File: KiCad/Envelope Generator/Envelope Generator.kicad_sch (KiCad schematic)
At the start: 43 parts, among them J1 Screw_Terminal_01x03, J2 Screw_Terminal_01x03, U1 TL074, U2 TL074, U3 TL074

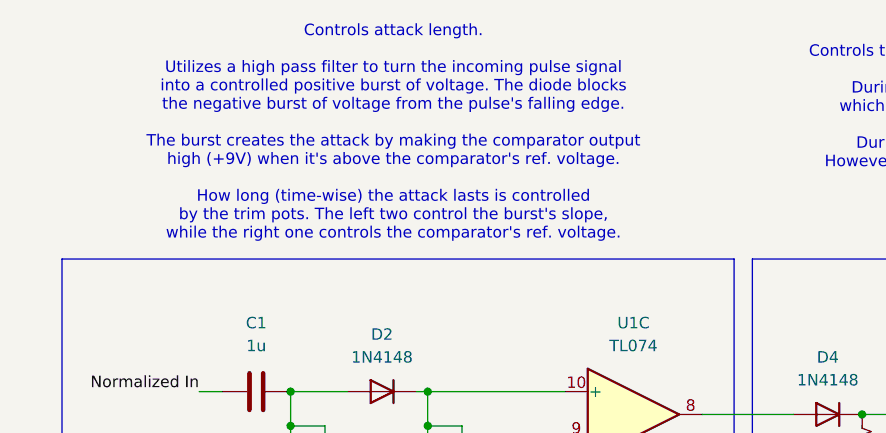
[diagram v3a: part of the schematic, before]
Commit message: fixed power board, replaced sketchy voltage divider - op amp cct. with an LDO to product +5V
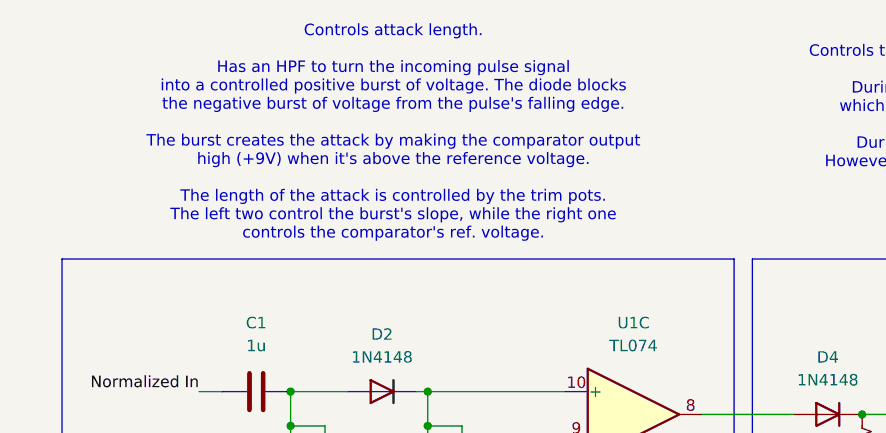
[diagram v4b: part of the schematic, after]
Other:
- note added: "Controls attack length. Has an HPF to turn the incoming pulse signal into a controlled positive burst of voltage. The diode blocks the negative burst of voltage from the pulse's falling edge. The burst creates the attack by making the comparator output high (+9V) when it's above the reference voltage. The length of the attack is controlled by the trim pots. The left two control the burst's slope,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"
- note removed: "Controls attack length. Utilizes a high pass filter to turn the incoming pulse signal into a controlled positive burst of voltage. The diode blocks the negative burst of voltage from the pulse's falling edge. The burst creates the attack by making the comparator output high (+9V) when it's above the comparator's ref. voltage. How long (time-wise) the attack lasts is controlled by the trim pots. T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"
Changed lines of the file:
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@@
 		)
 	)
-	(text "Controls attack length.\n\nUtilizes a high pass filter to turn the incoming pulse signal\ninto a controlled positive burst of voltage. The diode blocks\nthe negative burst of voltage from the pulse's falling edge.\n\nThe burst creates the attack by making the comparator output\nhigh (+9V) when it's above the comparator's ref. voltage.\n\nHow long (time-wise) the attack lasts is controlled\nby the trim pots. The left two control the burst's slope,\nwhile the right one controls the comparator's ref. voltage."
+	(text "Controls attack length.\n\nHas an HPF to turn the incoming pulse signal\ninto a controlled positive burst of voltage. The diode blocks\nthe negative burst of voltage from the pulse's falling edge.\n\nThe burst creates the attack by making the comparator output\nhigh (+9V) when it's above the reference voltage.\n\nThe length of the attack is controlled by the trim pots.\nThe left two control the burst's slope, while the right one\ncontrols the comparator's ref. voltage."
 		(exclude_from_sim no)
 		(at 59.69 27.178 0)

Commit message: finished separating into separate kicad projects
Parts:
- removed R1, R2: 100k, symbol Device:R_US
- added RV1: 100k, Potentiometer_THT:Potentiometer_Bourns_3296W_Vertical, symbol Device:R_Potentiometer_Trim_US
- renumbered R3 to R1, R4 to R2, R5 to R3, R6 to R4, R7 to R5, R8 to R6, R9 to R7, R10 to R8, RV9 to RV10, RV10 to RV11, RV11 to RV12, RV12 to RV13, RV13 to RV14, RV14 to RV15, RV1 to RV2, RV2 to RV3, RV3 to RV4, RV4 to RV5, RV5 to RV6, RV6 to RV7, RV7 to RV8, RV8 to RV9
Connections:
- net -9V: now also RV1.1
- net GND: now also RV1.3
- net at U1.2 (-): now also RV1.2
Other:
- note added: "Ref. voltage should be between -5V and -0.5V, however in case that's wrong, it's adjustable."
- note added: "Turns the input into a binary signal, low is 0V and high is 9V. This is needed because the input is not a binary signal, instead it is either -5V or a range between ~0V to ~2.5V since the input also serves as the oscillator's control voltage."
- note removed: "Trigger above -4.5V"
- note removed: "Turns the input into a binary signal, low is 0V and high is 9V. This is because the input is not a binary signal, instead it is either -9V or a range between ~0V to ~2.5V since the input also serves as the oscillator's control voltage."

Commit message: added test points
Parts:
- added TP? (x14): TestPoint_Small, symbol Connector:TestPoint_Small
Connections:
- net Amp Out: now also TP?.1
- net Amp Sustain/Base Voltage: now also TP?.1
- net Amp Target Voltage: now also TP?.1
- net Filter Out: now also TP?.1
- net Filter Sustain/Base Voltage: now also TP?.1
- net Filter Target Voltage: now also TP?.1
- net GND: now also TP?.1
- net In: now also TP?.1
- net Normalized In: now also TP?.1
- net Unscaled Amp Out: now also TP?.1
- net Unscaled Filter Out: now also TP?.1
- net Filter Burst: now reaches D5.2 (A), U1.7
- net Filter Burst: now also TP?.1
- net Input Comparator Ref: now reaches RV1.2, U1.2 (-)
- net Input Comparator Ref: now also TP?.1
- net Amp Burst: now reaches D4.2 (A), U1.8
- net Amp Burst: now also TP?.1
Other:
- moved on the sheet: C3, D1, R1, RV1, RV8, RV9, U1A, U1D

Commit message: added power indicator LEDs
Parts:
- gave numbers to parts that had none: 14
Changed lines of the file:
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@@
 		(dnp no)
 		(fields_autoplaced yes)
-		(property "Reference" "TP?"
+		(property "Reference" "TP10"
 			(at 194.31 153.6699 0)
 			(hide yes)
@@
 			(project "Envelope Generator"
 				(path "/f00ec82e-7fb8-4c7e-bfac-cc036a335e43"
-					(reference "TP?")
+					(reference "TP10")
 					(unit 1)
 				)
@@
 		(dnp no)
 		(fields_autoplaced yes)
-		(property "Reference" "TP?"
+		(property "Reference" "TP6"
 			(at 143.51 173.9899 0)
 			(hide yes)
@@
 			(project "Envelope Generator"
 				(path "/f00ec82e-7fb8-4c7e-bfac-cc036a335e43"
-					(reference "TP?")
+					(reference "TP6")
 					(unit 1)
 				)
@@
 		(dnp no)
 		(fields_autoplaced yes)
-		(property "Reference" "TP?"
+		(property "Reference" "TP4"
 			(at 97.79 160.0199 0)
 			(hide yes)
@@
 			(project "Envelope Generator"
 				(path "/f00ec82e-7fb8-4c7e-bfac-cc036a335e43"
-					(reference "TP?")
+					(reference "TP4")
 					(unit 1)
 				)
@@
 		(dnp no)
 		(fields_autoplaced yes)
-		(property "Reference" "TP?"
+		(property "Reference" "TP1"
 			(at 36.83 163.8299 0)
 			(hide yes)
@@
 			(project "Envelope Generator"
 				(path "/f00ec82e-7fb8-4c7e-bfac-cc036a335e43"
-					(reference "TP?")
+					(reference "TP1")
 					(unit 1)
 				)
@@
 		(dnp no)
 		(fields_autoplaced yes)
-		(property "Reference" "TP?"
+		(property "Reference" "TP13"
 			(at 227.33 132.0799 0)
 			(hide yes)
@@
 			(project "Envelope Generator"
 				(path "/f00ec82e-7fb8-4c7e-bfac-cc036a335e43"
-					(reference "TP?")
+					(reference "TP13")
 					(unit 1)
 				)
@@
 		(dnp no)
 		(fields_autoplaced yes)
-		(property "Reference" "TP?"
+		(property "Reference" "TP2"
 			(at 96.52 57.1499 0)
 			(hide yes)
@@
 			(project "Envelope Generator"
 				(path "/f00ec82e-7fb8-4c7e-bfac-cc036a335e43"
-					(reference "TP?")
+					(reference "TP2")
 					(unit 1)
 				)
@@
 		(dnp no)
 		(fields_autoplaced yes)
-		(property "Reference" "TP?"
+		(property "Reference" "TP9"
 			(at 194.31 151.1299 0)
 			(hide yes)
@@
 			(project "Envelope Generator"
 				(path "/f00ec82e-7fb8-4c7e-bfac-cc036a335e43"
-					(reference "TP?")
+					(reference "TP9")
 					(unit 1)
 				)
@@
 		(dnp no)
 		(fields_autoplaced yes)
-		(property "Reference" "TP?"
+		(property "Reference" "TP5"
 			(at 143.51 148.5899 0)
 			(hide yes)
@@
 			(project "Envelope Generator"
 				(path "/f00ec82e-7fb8-4c7e-bfac-cc036a335e43"
-					(reference "TP?")
+					(reference "TP5")
 					(unit 1)
 				)
@@
 		(dnp no)
 		(fields_autoplaced yes)
-		(property "Reference" "TP?"
+		(property "Reference" "TP12"
 			(at 227.33 76.1999 0)
 			(hide yes)
@@
 			(project "Envelope Generator"
 				(path "/f00ec82e-7fb8-4c7e-bfac-cc036a335e43"
-					(reference "TP?")
+					(reference "TP12")
 					(unit 1)
 				)
@@
 		(dnp no)
 		(fields_autoplaced yes)
-		(property "Reference" "TP?"
+		(property "Reference" "TP14"
 			(at 234.442 153.6699 0)
 			(hide yes)
@@
 			(project "Envelope Generator"
 				(path "/f00ec82e-7fb8-4c7e-bfac-cc036a335e43"
-					(reference "TP?")
+					(reference "TP14")
 					(unit 1)
 				)
@@
 		(dnp no)
 		(fields_autoplaced yes)
-		(property "Reference" "TP?"
+		(property "Reference" "TP11"
 			(at 194.31 156.2099 0)
 			(hide yes)
@@
 			(project "Envelope Generator"
 				(path "/f00ec82e-7fb8-4c7e-bfac-cc036a335e43"
-					(reference "TP?")
+					(reference "TP11")
 					(unit 1)
 				)
@@
 		(dnp no)
 		(fields_autoplaced yes)
-		(property "Reference" "TP?"
+		(property "Reference" "TP7"
 			(at 158.75 59.6899 0)
 			(hide yes)
@@
 			(project "Envelope Generator"
 				(path "/f00ec82e-7fb8-4c7e-bfac-cc036a335e43"
-					(reference "TP?")
+					(reference "TP7")
 					(unit 1)
 				)
@@
 		(dnp no)
 		(fields_autoplaced yes)
-		(property "Reference" "TP?"
+		(property "Reference" "TP8"
 			(at 160.02 115.5699 0)
 			(hide yes)
@@
 			(project "Envelope Generator"
 				(path "/f00ec82e-7fb8-4c7e-bfac-cc036a335e43"
-					(reference "TP?")
+					(reference "TP8")
 					(unit 1)
 				)
@@
 		(dnp no)
 		(fields_autoplaced yes)
-		(property "Reference" "TP?"
+		(property "Reference" "TP3"
 			(at 96.52 113.0299 0)
 			(hide yes)
@@
 			(project "Envelope Generator"
 				(path "/f00ec82e-7fb8-4c7e-bfac-cc036a335e43"
-					(reference "TP?")
+					(reference "TP3")
 					(unit 1)
 				)

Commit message: updated footprints in envelope generator
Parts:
- C3: footprint (none) -> Capacitor_SMD:C_0805_2012Metric
- J1, J2: footprint (none) -> Header 691137710003:691137710003
- R1, R4, R5, R6, R7, R8: footprint (none) -> Resistor_SMD:R_0805_2012Metric
- R2, R3: footprint Resistor_SMD:R_0603_1608Metric -> Resistor_SMD:R_0805_2012Metric
- RV1, RV6, RV7: footprint Potentiometer_THT:Potentiometer_Bourns_3296W_Vertical -> Potentiometer_THT:Potentiometer_Bourns_3339P_Vertical
- RV10, RV11, RV12, RV13, RV14, RV15, RV2, RV3, RV4, RV5: footprint (none) -> Potentiometer_THT:Potentiometer_Bourns_3339P_Vertical
- RV8, RV9: footprint Potentiometer_SMD:Potentiometer_Bourns_TC33X_Vertical -> Potentiometer_THT:Potentiometer_Bourns_3339P_Vertical
- TP1, TP10, TP11, TP12, TP13, TP14, TP2, TP3, TP4, TP5, TP6, TP7, TP8, TP9: footprint (none) -> TestPoint:TestPoint_Keystone_5000-5004_Miniature
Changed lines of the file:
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@@
 			)
 		)
-		(property "Footprint" "Potentiometer_SMD:Potentiometer_Bourns_TC33X_Vertical"
+		(property "Footprint" "Potentiometer_THT:Potentiometer_Bourns_3339P_Vertical"
 			(at 142.24 160.02 0)
 			(hide yes)
@@
 			)
 		)
-		(property "Footprint" ""
+		(property "Footprint" "Resistor_SMD:R_0805_2012Metric"
 			(at 189.484 52.324 90)
 			(hide yes)
@@
 			)
 		)
-		(property "Footprint" ""
+		(property "Footprint" "Potentiometer_THT:Potentiometer_Bourns_3339P_Vertical"
 			(at 234.95 119.38 0)
 			(hide yes)
@@
 			)
 		)
-		(property "Footprint" ""
+		(property "Footprint" "TestPoint:TestPoint_Keystone_5000-5004_Miniature"
 			(at 198.12 154.94 0)
 			(hide yes)
@@
 			)
 		)
-		(property "Footprint" "Potentiometer_THT:Potentiometer_Bourns_3296W_Vertical"
+		(property "Footprint" "Potentiometer_THT:Potentiometer_Bourns_3339P_Vertical"
 			(at 78.74 125.73 0)
 			(hide yes)
@@
 			)
 		)
-		(property "Footprint" ""
+		(property "Footprint" "TestPoint:TestPoint_Keystone_5000-5004_Miniature"
 			(at 147.32 175.26 0)
 			(hide yes)
@@
 			)
 		)
-		(property "Footprint" ""
+		(property "Footprint" "TestPoint:TestPoint_Keystone_5000-5004_Miniature"
 			(at 101.6 161.29 0)
 			(hide yes)
@@
 			)
 		)
-		(property "Footprint" ""
+		(property "Footprint" "TestPoint:TestPoint_Keystone_5000-5004_Miniature"
 			(at 40.64 165.1 0)
 			(hide yes)
@@
 			)
 		)
-		(property "Footprint" "Resistor_SMD:R_0603_1608Metric"
+		(property "Footprint" "Resistor_SMD:R_0805_2012Metric"
 			(at 112.776 118.364 90)
 			(hide yes)
@@
 			)
 		)
-		(property "Footprint" ""
+		(property "Footprint" "TestPoint:TestPoint_Keystone_5000-5004_Miniature"
 			(at 231.14 133.35 0)
 			(hide yes)
@@
 			)
 		)
-		(property "Footprint" ""
+		(property "Footprint" "Resistor_SMD:R_0805_2012Metric"
 			(at 189.484 108.204 90)
 			(hide yes)
@@
 			)
 		)
-		(property "Footprint" ""
+		(property "Footprint" "Potentiometer_THT:Potentiometer_Bourns_3339P_Vertical"
 			(at 63.5 64.77 0)
 			(hide yes)
@@
 			)
 		)
-		(property "Footprint" ""
+		(property "Footprint" "Resistor_SMD:R_0805_2012Metric"
 			(at 61.976 162.814 90)
 			(hide yes)
@@
 			)
 		)
-		(property "Footprint" ""
+		(property "Footprint" "TestPoint:TestPoint_Keystone_5000-5004_Miniature"
 			(at 100.33 58.42 0)
 			(hide yes)
@@
 			)
 		)
-		(property "Footprint" ""
+		(property "Footprint" "TestPoint:TestPoint_Keystone_5000-5004_Miniature"
 			(at 198.12 152.4 0)
 			(hide yes)
@@
 			)
 		)
-		(property "Footprint" ""
+		(property "Footprint" "TestPoint:TestPoint_Keystone_5000-5004_Miniature"
 			(at 147.32 149.86 0)
 			(hide yes)
@@
 			)
 		)
-		(property "Footprint" ""
+		(property "Footprint" "TestPoint:TestPoint_Keystone_5000-5004_Miniature"
 			(at 231.14 77.47 0)
 			(hide yes)
@@
 			)
 		)
-		(property "Footprint" ""
+		(property "Footprint" "TestPoint:TestPoint_Keystone_5000-5004_Miniature"
 			(at 238.252 154.94 0)
 			(hide yes)
@@
 			)
 		)
-		(property "Footprint" "Potentiometer_THT:Potentiometer_Bourns_3296W_Vertical"
+		(property "Footprint" "Potentiometer_THT:Potentiometer_Bourns_3339P_Vertical"
 			(at 35.56 171.45 0)
 			(hide yes)
@@
 			)
 		)
-		(property "Footprint" ""
+		(property "Footprint" "TestPoint:TestPoint_Keystone_5000-5004_Miniature"
 			(at 198.12 157.48 0)
 			(hide yes)
@@
 			)
 		)
-		(property "Footprint" ""
+		(property "Footprint" "Header 691137710003:691137710003"
 			(at 240.03 154.94 0)
 			(hide yes)
@@
 			)
 		)
-		(property "Footprint" ""
+		(property "Footprint" "TestPoint:TestPoint_Keystone_5000-5004_Miniature"
 			(at 162.56 60.96 0)
 			(hide yes)
@@
 			)
 		)
-		(property "Footprint" ""
+		(property "Footprint" "Potentiometer_THT:Potentiometer_Bourns_3339P_Vertical"
 			(at 48.26 119.38 0)
 			(hide yes)
@@
 			)
 		)
-		(property "Footprint" ""
+		(property "Footprint" "Potentiometer_THT:Potentiometer_Bourns_3339P_Vertical"
 			(at 179.07 53.34 0)
 			(hide yes)
@@
 			)
 		)
-		(property "Footprint" ""
+		(property "Footprint" "Potentiometer_THT:Potentiometer_Bourns_3339P_Vertical"
 			(at 179.07 68.58 0)
 			(hide yes)
@@
 			)
 		)
-		(property "Footprint" ""
+		(property "Footprint" "Potentiometer_THT:Potentiometer_Bourns_3339P_Vertical"
 			(at 179.07 109.22 0)
 			(hide yes)
@@
 			)
 		)
-		(property "Footprint" ""
+		(property "Footprint" "TestPoint:TestPoint_Keystone_5000-5004_Miniature"
 			(at 163.83 116.84 0)
 			(hide yes)
@@
 			)
 		)
-		(property "Footprint" ""
+		(property "Footprint" "Header 691137710003:691137710003"
 			(at 199.39 154.94 0)
 			(hide yes)
@@
 			)
 		)
-		(property "Footprint" ""
+		(property "Footprint" "Capacitor_SMD:C_0805_2012Metric"
 			(at 71.12 162.56 0)
 			(hide yes)
@@
 			)
 		)
-		(property "Footprint" ""
+		(property "Footprint" "Resistor_SMD:R_0805_2012Metric"
 			(at 232.664 62.484 90)
 			(hide yes)
@@
 			)
 		)
-		(property "Footprint" ""
+		(property "Footprint" "Resistor_SMD:R_0805_2012Metric"
 			(at 189.484 67.564 90)
 			(hide yes)
@@
 			)
 		)
-		(property "Footprint" "Potentiometer_THT:Potentiometer_Bourns_3296W_Vertical"
+		(property "Footprint" "Potentiometer_THT:Potentiometer_Bourns_3339P_Vertical"
 			(at 78.74 69.85 0)
 			(hide yes)
@@
 			)
 		)
-		(property "Footprint" ""
+		(property "Footprint" "Potentiometer_THT:Potentiometer_Bourns_3339P_Vertical"
 			(at 179.07 124.46 0)
 			(hide yes)
@@
 			)
 		)
-		(property "Footprint" "Resistor_SMD:R_0603_1608Metric"
+		(property "Footprint" "Resistor_SMD:R_0805_2012Metric"
 			(at 112.776 62.484 90)
 			(hide yes)
@@
 			)
 		)
-		(property "Footprint" ""
+		(property "Footprint" "Potentiometer_THT:Potentiometer_Bourns_3339P_Vertical"
 			(at 63.5 119.38 0)
 			(hide yes)
@@
 			)
 		)
-		(property "Footprint" ""
+		(property "Footprint" "TestPoint:TestPoint_Keystone_5000-5004_Miniature"
 			(at 100.33 114.3 0)
 			(hide yes)
@@
 			)
 		)
-		(property "Footprint" ""
+		(property "Footprint" "Potentiometer_THT:Potentiometer_Bourns_3339P_Vertical"
 			(at 245.11 54.61 0)
 			(hide yes)
@@
 			)
 		)
-		(property "Footprint" "Potentiometer_SMD:Potentiometer_Bourns_TC33X_Vertical"
+		(property "Footprint" "Potentiometer_THT:Potentiometer_Bourns_3339P_Vertical"
 			(at 142.24 185.42 0)
 			(hide yes)
@@
 			)
 		)
-		(property "Footprint" ""
+		(property "Footprint" "Resistor_SMD:R_0805_2012Metric"
 			(at 189.484 123.444 90)
 			(hide yes)
@@
 			)
 		)
-		(property "Footprint" ""
+		(property "Footprint" "Potentiometer_THT:Potentiometer_Bourns_3339P_Vertical"
 			(at 48.26 64.77 0)
 			(hide yes)
